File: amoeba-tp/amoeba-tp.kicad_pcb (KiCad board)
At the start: 2 copper layers, 56.9 x 35.2 mm, 55 parts

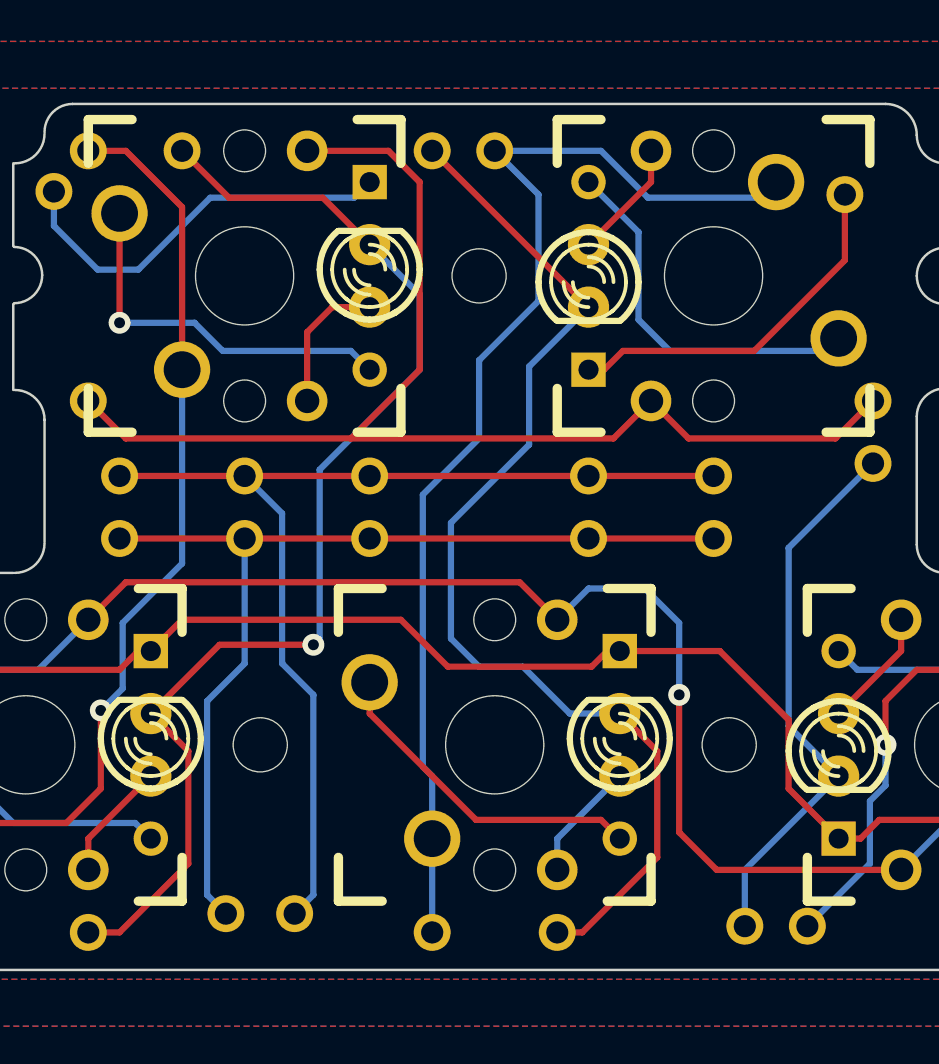
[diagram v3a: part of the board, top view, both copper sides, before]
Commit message: Fixes for Oshpark submission and minor labeling adjustments.
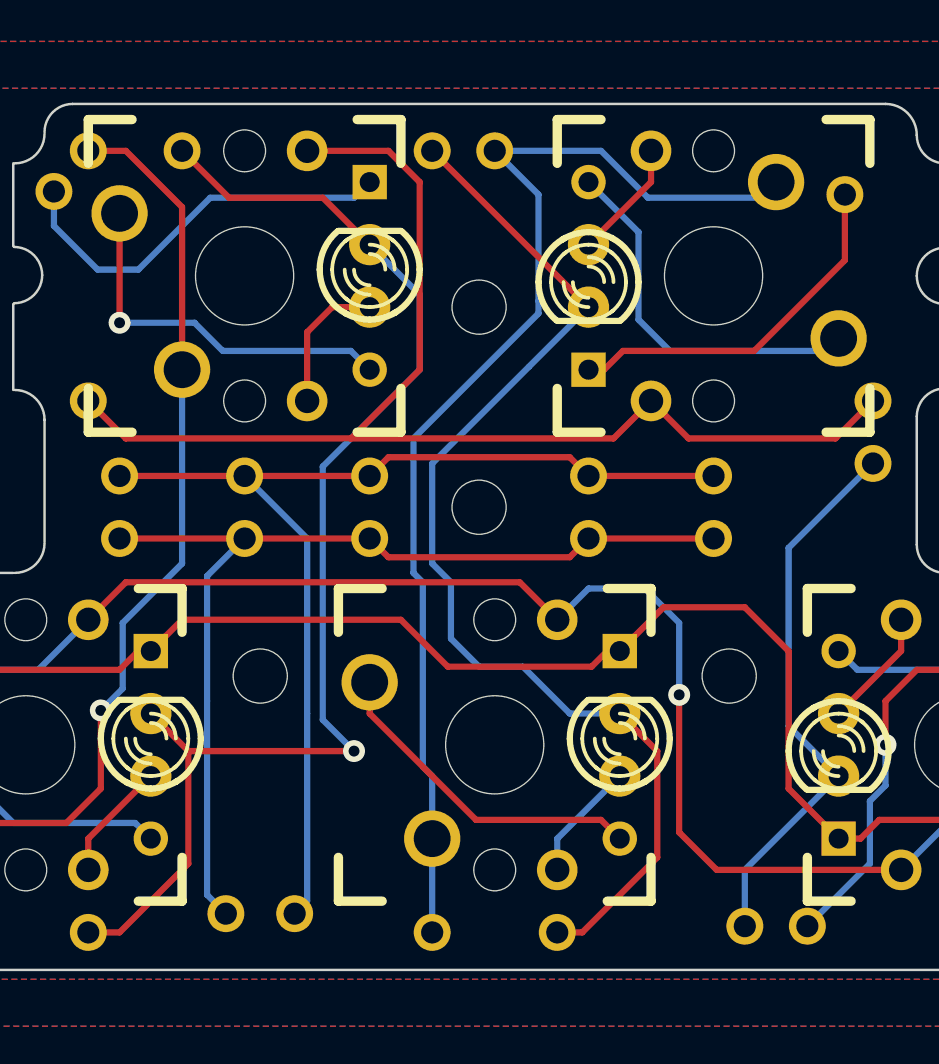
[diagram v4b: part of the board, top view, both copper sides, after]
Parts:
- added ?: , M2, F.Cu at (123.8, 127.5)
- moved ? 2.79 mm to (114.9, 134.4)
- moved ? 2.79 mm to (134.0, 134.4)
- moved ? 1.27 mm to (123.8, 119.4)
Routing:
- net /key:H/LC0: track 47.8 -> 51.5 mm
- net /key:B/SR0: track 61.5 -> 64.6 mm
- net N-0000012: track 40.3 -> 40.9 mm
- net /key:B/LC0: track 44.7 -> 45.3 mm

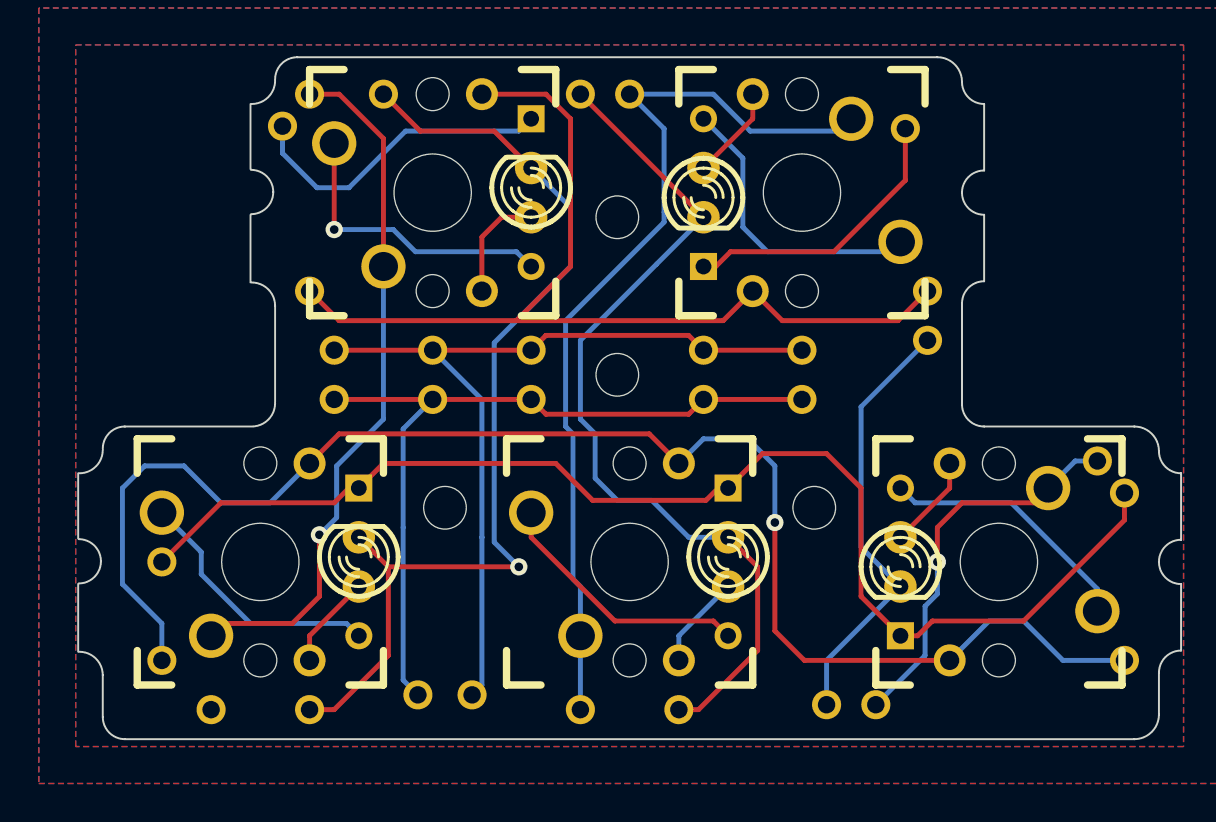
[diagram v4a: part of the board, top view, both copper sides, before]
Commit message: Adding SMD options to TP module.
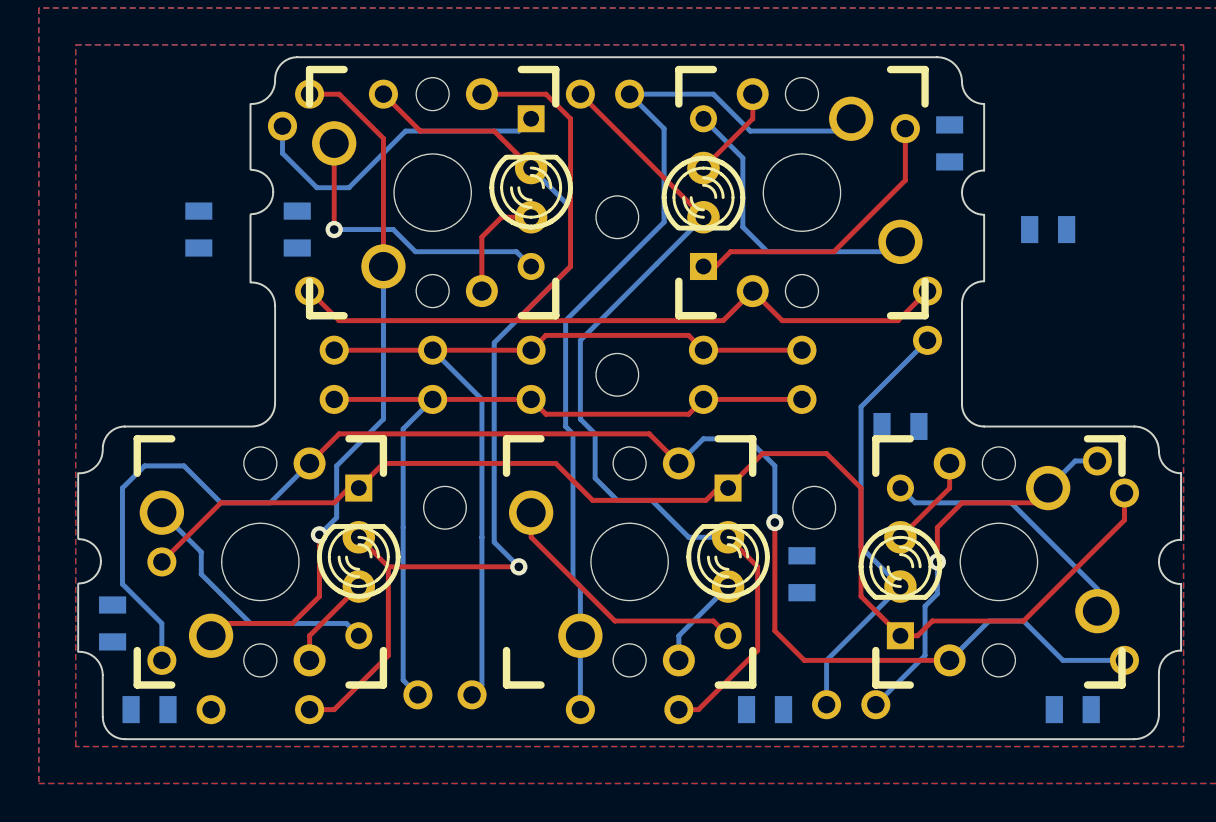
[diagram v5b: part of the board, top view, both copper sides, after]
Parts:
- removed D0:0, D0:1, D1:0, D1:1, D2:1: DIODE, D3
- removed R0:0, R0:1, R1:0, R1:1, R2:1: RESISTOR, RESISTOR
- added D0:0:0: DIODE, D3, B.Cu at (119.4, 118.1)
- added D0:0:1: DIODE, SM0805D, B.Cu at (107.3, 120.0)
- added D0:1:0: DIODE, D3, B.Cu at (128.3, 118.1)
- added D0:1:1: DIODE, SM0805D, B.Cu at (141.0, 115.6)
- added D1:0:0: DIODE, D3, B.Cu at (138.4, 137.2)
- added D1:0:1: DIODE, SM0805D, B.Cu at (138.4, 130.2)
- added D1:1:0: DIODE, D3, B.Cu at (129.5, 137.2)
- added D1:1:1: DIODE, SM0805D, B.Cu at (133.3, 137.8)
- added D2:1:0: DIODE, D3, B.Cu at (110.5, 137.2)
- added D2:1:1: DIODE, SM0805D, B.Cu at (97.8, 140.3)
- added R0:0:0: RESISTOR, RESISTOR, B.Cu at (130.8, 118.1)
- added R0:0:1: RESISTOR, SM0805, B.Cu at (102.2, 120.0)
- added R0:1:0: RESISTOR, RESISTOR, B.Cu at (116.8, 118.1)
- added R0:1:1: RESISTOR, SM0805, B.Cu at (146.1, 120.0)
- added R1:0:0: RESISTOR, RESISTOR, B.Cu at (141.0, 137.2)
- added R1:0:1: RESISTOR, SM0805, B.Cu at (147.3, 144.8)
- added R1:1:0: RESISTOR, RESISTOR, B.Cu at (127.0, 137.2)
- added R1:1:1: RESISTOR, SM0805, B.Cu at (131.4, 144.8)
- added R2:1:0: RESISTOR, RESISTOR, B.Cu at (108.0, 137.2)
- added R2:1:1: RESISTOR, SM0805, B.Cu at (99.7, 144.8)
- moved S0:1 38.1 mm to (143.5, 137.2), turned to 270 degrees
- moved S2:1 38.1 mm to (105.4, 137.2), turned to 90 degrees
- moved S0:0 19.0 mm to (133.3, 118.1), turned to 270 degrees
- moved S1:0 19.0 mm to (114.3, 118.1), turned to 90 degrees
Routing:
- net /key:B/LR0: track 76.7 -> 102.8 mm
- net /key:G/LR0: track 51.1 -> 25.0 mm
- net /key:B/SC0: track 47.4 -> 67.0 mm, vias 0 -> 1
- net /key:H/SC0: track 36.2 -> 22.4 mm
- net /key:G/SR0: track 31.4 -> 39.4 mm
- net /key:B/SR0: track 64.6 -> 56.5 mm
- net /key:V/SC0: track 20.1 -> 14.3 mm, vias 1 -> 0
- net N-0000021: track 5.75 -> 2.79 mm
- net N-0000015: track 4.86 -> 7.82 mm
- net N-0000016: track 13.5 -> 15.7 mm
- net N-0000022: track 15.4 -> 13.4 mm, vias 1 -> 0
- net N-0000014: track 15.3 -> 15.1 mm, vias 0 -> 1

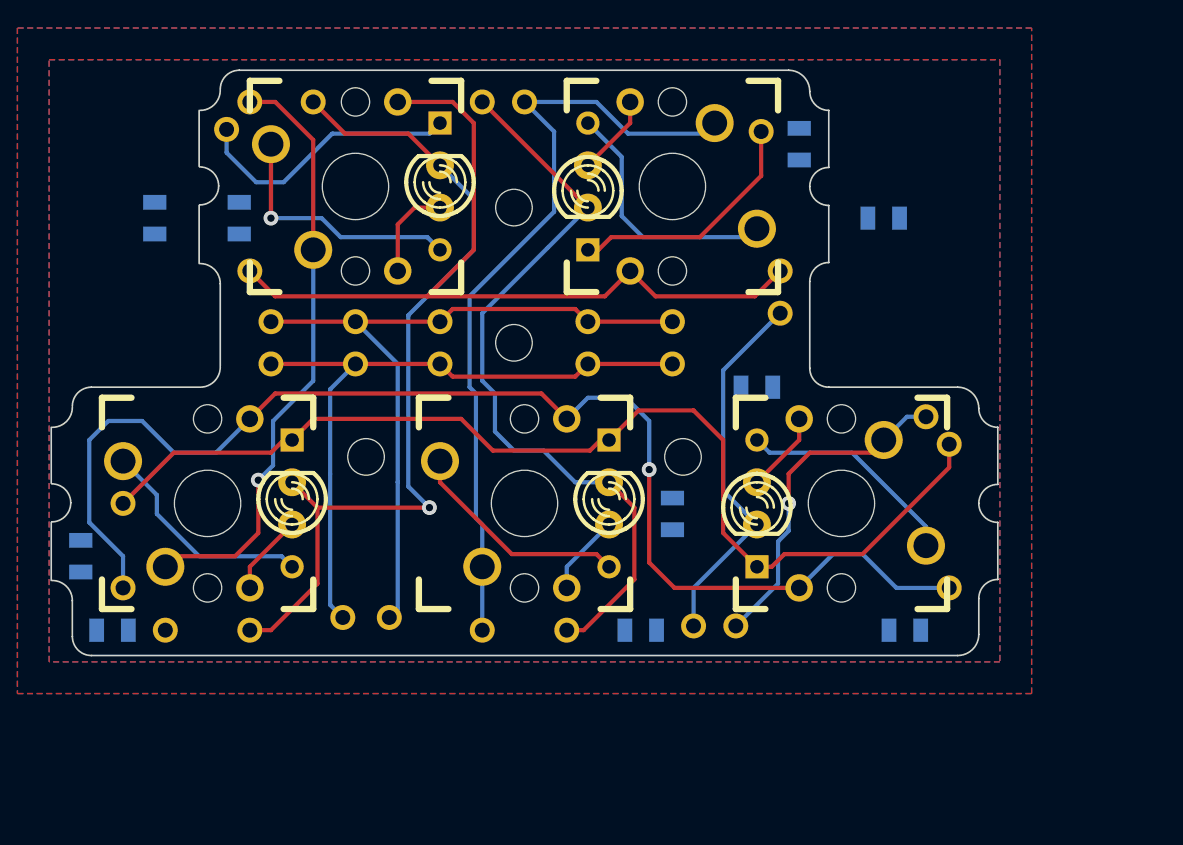
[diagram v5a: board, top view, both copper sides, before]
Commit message: Adding mouse buttons PCB.
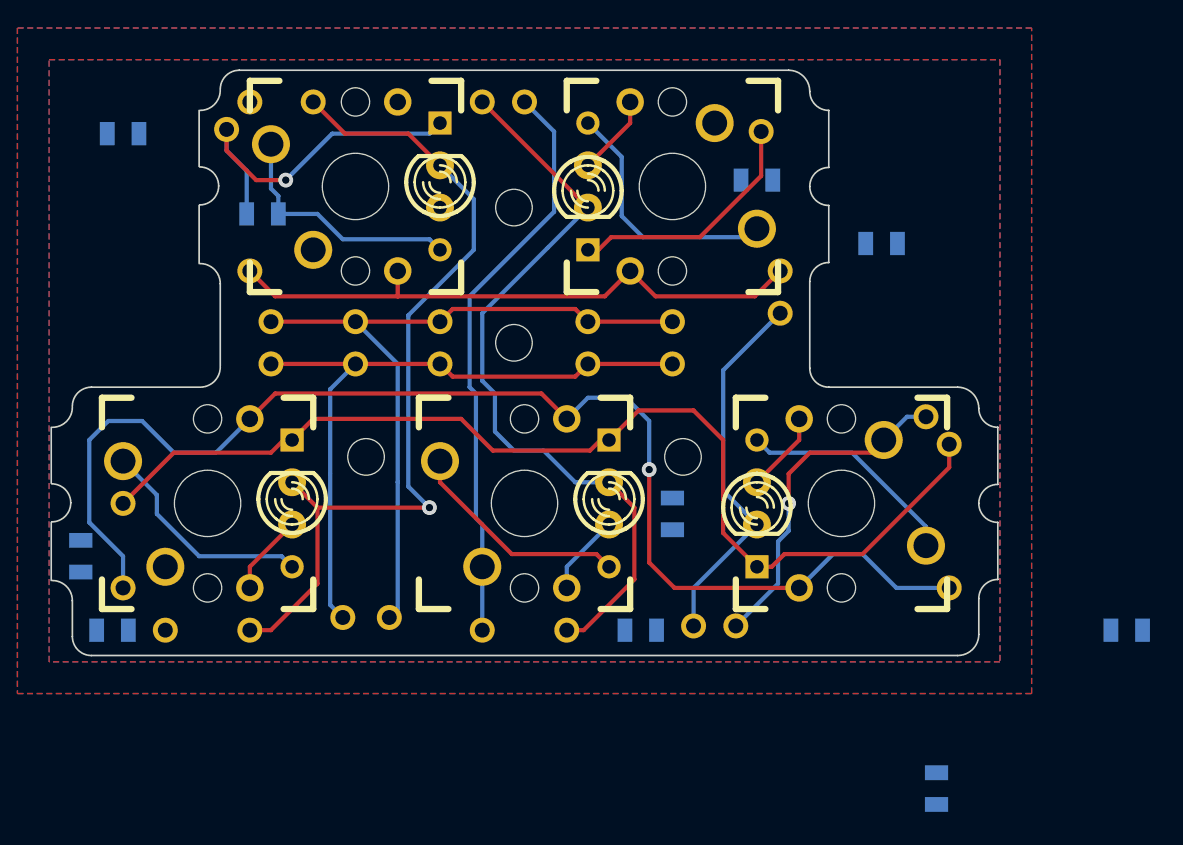
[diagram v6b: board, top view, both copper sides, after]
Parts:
- moved R1:0:1 55.7 mm to (100.3, 114.9)
- moved R0:0:1 43.7 mm to (145.9, 121.5), turned to 0 degrees
- moved D0:1:1 39.6 mm to (149.2, 154.3)
- moved D1:0:1 31.5 mm to (108.7, 119.8)
- moved D0:0:1 31.2 mm to (138.4, 117.7), turned to 180 degrees
- moved R0:1:0 30.7 mm to (141.0, 137.2)
- moved R1:0:0 30.7 mm to (116.8, 118.1)
- moved R0:1:1 28.8 mm to (160.7, 144.8)
- moved D1:0:0 26.9 mm to (119.4, 118.1), turned to 90 degrees
- moved D0:1:0 21.6 mm to (138.4, 137.2)
- moved D0:0:0 8.89 mm to (128.3, 118.1), turned to 270 degrees
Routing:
- net /key:B/LR0: track 102.8 -> 67.6 mm
- net /key:B/SC0: track 67.0 -> 34.9 mm, vias 1 -> 0
- net /key:G/LR0: track 25.0 -> 35.9 mm
- net /key:V/SC0: track 14.3 -> 4.74 mm
- net /key:B/SR0: track 56.5 -> 64.6 mm
- net /key:H/SC0: track 22.4 -> 15.4 mm
- net N-0000015: track 7.82 -> 14.0 mm
- net /key:G/SR0: track 39.4 -> 36.8 mm, vias 0 -> 1
- net N-0000016: track 15.7 -> 13.5 mm
- net N-0000022: track 13.4 -> 15.3 mm
- net N-0000021: track 2.79 -> 1.27 mm
- net N-0000013: track 4.86 -> 3.59 mm
- net N-0000014: track 15.1 -> 15.0 mm, vias 1 -> 0
